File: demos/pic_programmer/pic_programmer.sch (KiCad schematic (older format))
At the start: 56 parts, among them J1 DB9-FEMAL, P1 CONN_2, P101 CONN_1, P102 CONN_1, P103 CONN_1, P104 CONN_1, P105 CONN_1, P106 CONN_1, Q1 BC237, Q2 BC307, Q3 BC307, U2 74HC125, U3 7805, U4 LT1373

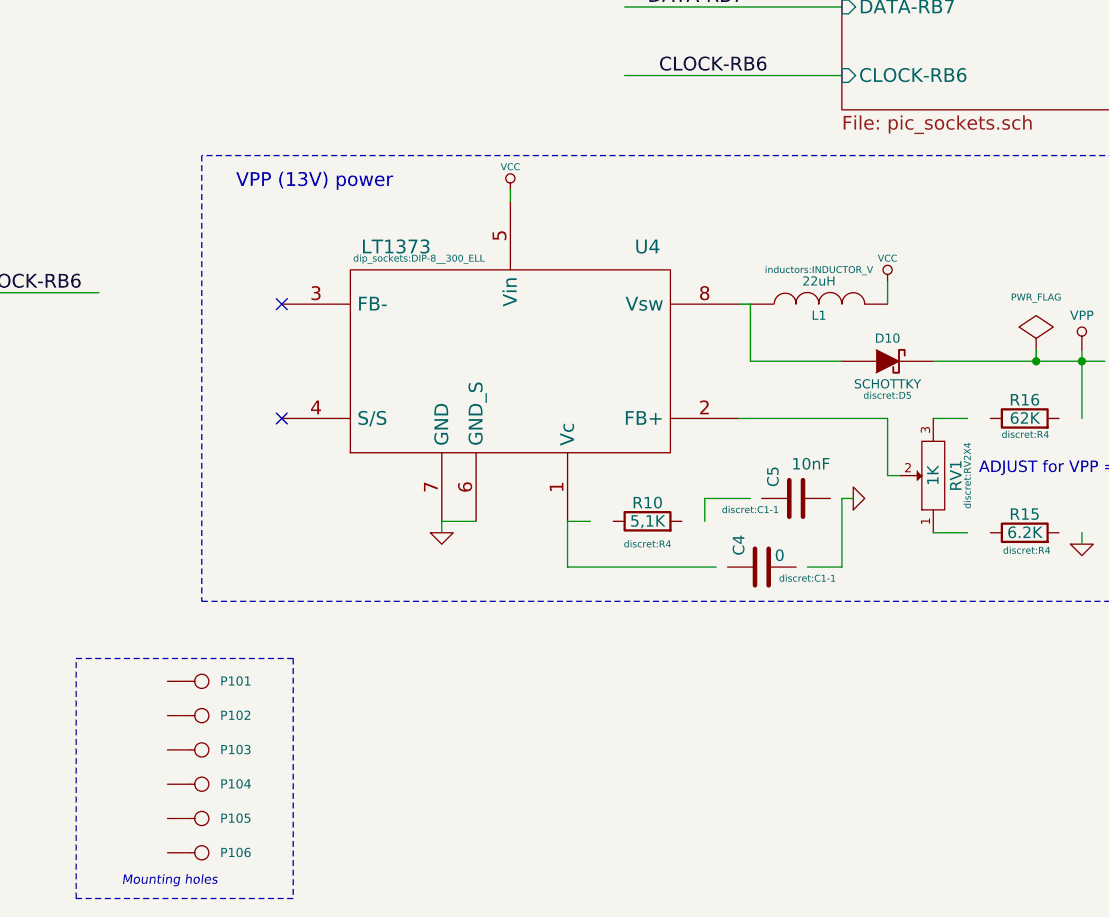
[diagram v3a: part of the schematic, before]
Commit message: demos/ schematic tidying
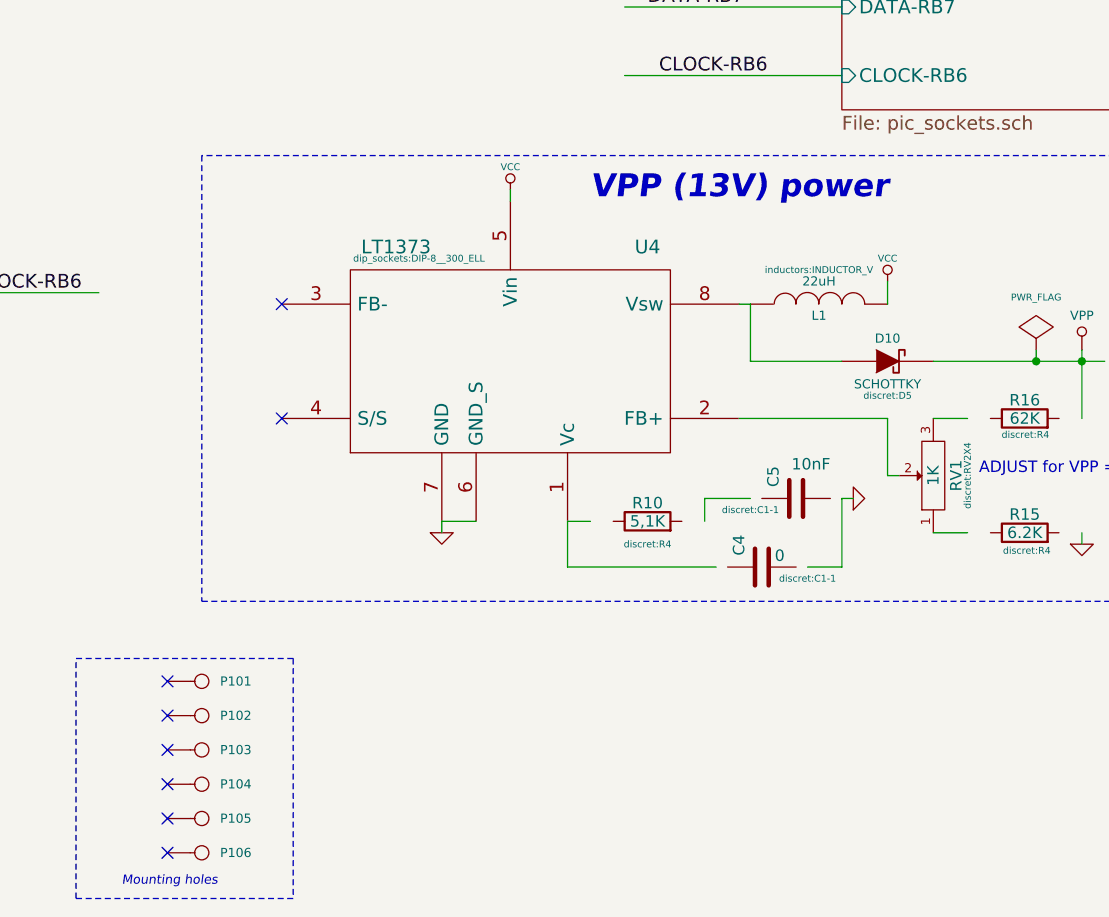
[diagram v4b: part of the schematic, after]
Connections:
- no-connect marks 6 -> 12
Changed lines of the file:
@@
 LIBS:xilinx
 LIBS:pic_programmer-cache
-EELAYER 24 0
+EELAYER 25 0
 EELAYER END
 $Descr A4 11693 8268
@@
 	1    0    0    -1
 $EndComp
-Text Notes 6550 4650 0    60   ~ 0
+Text Notes 8100 4700 0    100  Italic 20
 VPP (13V) power
 $Comp
@@
 Text Notes 6050 7700 0    40   Italic 0
 Mounting holes
+NoConn ~ 6250 6800
+NoConn ~ 6250 6950
+NoConn ~ 6250 7100
+NoConn ~ 6250 7250
+NoConn ~ 6250 7400
+NoConn ~ 6250 7550
 $EndSCHEMATC

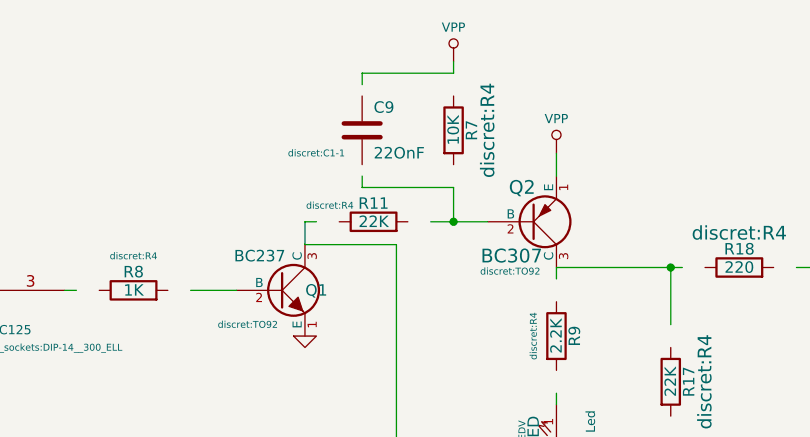
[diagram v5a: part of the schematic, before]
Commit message: Netlist generator: avoid changing the order of parts in libparts section each time libraries are reloaded. pic_programmer demo: very minor fix and update netlist. cached_container.cpp:  more info when the message "Out of memory" is displayed.
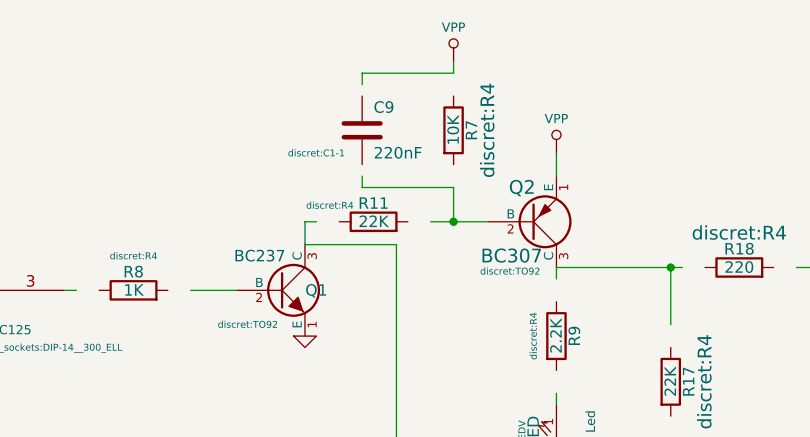
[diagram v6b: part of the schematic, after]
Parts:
- C9: value 22OnF -> 220nF
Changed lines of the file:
@@
 P 5700 1000
 F 0 "C9" H 5750 1100 50  0000 L CNN
-F 1 "22OnF" H 5750 900 50  0000 L CNN
+F 1 "220nF" H 5750 900 50  0000 L CNN
 F 2 "discret:C1-1" H 5500 900 30  0000 C CNN
 F 3 "" H 5700 1000 60  0001 C CNN

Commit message: merge from production bzr6934 to bzr 6953
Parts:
- C1, C2: footprint discret:CP10 -> Discret:CP10
- C3: footprint discret:CP8 -> Discret:CP8
- C4, C5, C9: footprint discret:C1-1 -> Discret:C1-1
- D1: footprint discret:D5 -> Discret:D5; symbol DIODE -> D
- D10: footprint discret:D5 -> Discret:D5; symbol DIODESCH -> D_Schottky
- D11, D2, D3, D4, D5, D6, D7: footprint discret:D3 -> Discret:D3; symbol DIODESCH -> D_Schottky
- D12, D8, D9: footprint discret:LEDV -> Discret:LEDV
- Q1, Q2, Q3: footprint discret:TO92 -> Discret:TO92
- R1, R10, R11, R12, R13, R14, R15, R16, R17, R18, R19, R2, R20, R21, R3, R4, R5, R6, R7, R8, R9: footprint discret:R4 -> Discret:R4
- RV1: footprint discret:RV2X4 -> Discret:RV2X4
- U3: footprint discret:LM78XX -> Discret:LM78XX
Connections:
- wire segments 95 -> 106
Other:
- moved on the sheet: R17
